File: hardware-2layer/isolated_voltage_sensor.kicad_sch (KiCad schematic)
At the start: 17 parts, among them U4 MCP41100, U5 LM358

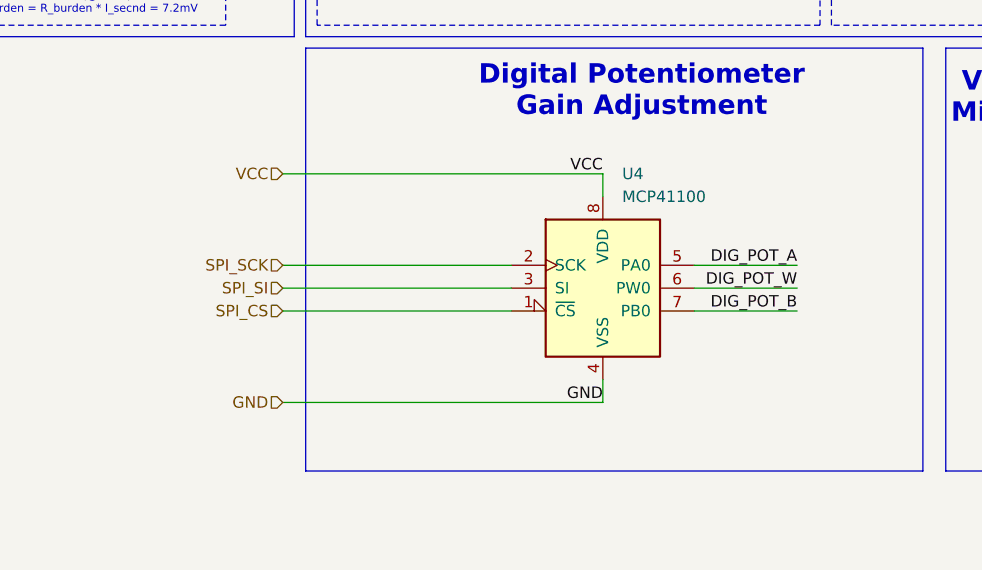
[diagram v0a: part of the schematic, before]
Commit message: updated board, last push before change to CRVR
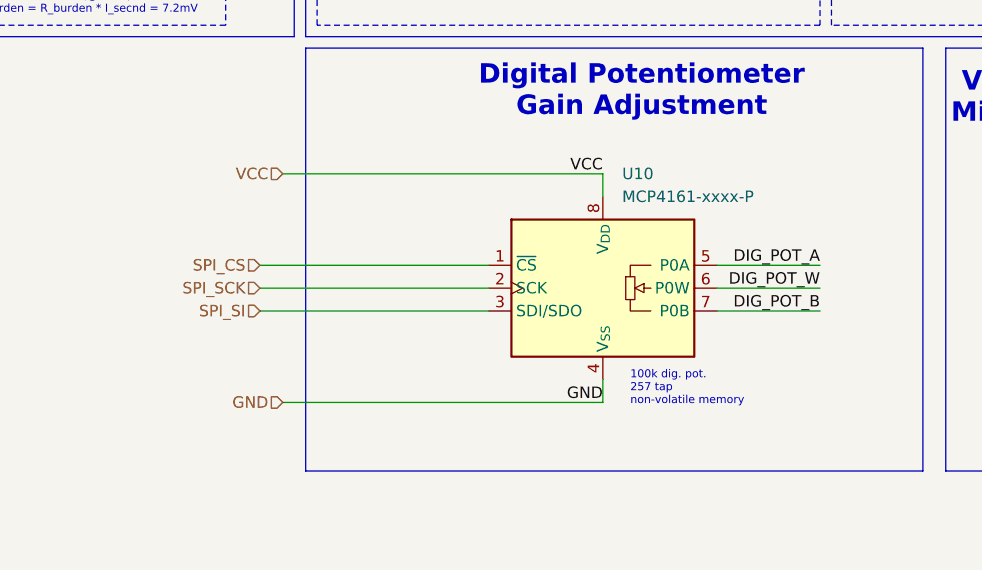
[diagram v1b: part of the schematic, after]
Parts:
- removed U4: MCP41100, symbol Potentiometer_Digital:MCP41100
- added U10: MCP4161-xxxx-P, Package_DIP:DIP-8_W7.62mm, symbol Potentiometer_Digital:MCP4161-xxxx-P
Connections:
- net DIG_POT_A: now also U10.5 (P0A)
- net DIG_POT_W: now also U10.6 (P0W)
- net GND: now also U10.4 (V_{SS}), U10.7 (P0B)
- net SPI_CS: now also U10.1 (~{CS})
- net SPI_SCK: now also U10.2 (SCK)
- net SPI_SI: now also U10.3 (SDI/SDO)
- net VCC: now also U10.8 (V_{DD})
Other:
- note added: "100k dig. pot. 257 tap non-volatile memory"
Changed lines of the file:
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@@
+		)
+	)
+	(text "100k dig. pot.\n257 tap\nnon-volatile memory"
+		(exclude_from_sim no)
+		(at 147.828 149.606 0)
+		(effects
+			(font
+				(size 0.889 0.889)
+				(thickness 0.0794)
+			)
+			(justify left)
 		)
 	)
@@
 	(wire
 		(pts
-			(xy 166.37 135.89) (xy 154.94 135.89)
+			(xy 168.91 135.89) (xy 157.48 135.89)
 		)
 		(stroke
@@
 	(wire
 		(pts
-			(xy 109.22 135.89) (xy 134.62 135.89)
+			(xy 106.68 138.43) (xy 132.08 138.43)
 		)
 		(stroke
@@
 	(wire
 		(pts
-			(xy 109.22 138.43) (xy 134.62 138.43)
+			(xy 106.68 140.97) (xy 132.08 140.97)
 		)
 		(stroke
@@
 	(wire
 		(pts
-			(xy 166.37 140.97) (xy 154.94 140.97)
+			(xy 168.91 140.97) (xy 157.48 140.97)
 		)
 		(stroke
@@
 	(wire
 		(pts
-			(xy 166.37 138.43) (xy 154.94 138.43)
-		)
-		(stroke
-			(width 0)
-			(type default)
-		)
-	)
-	(wire
-		(pts
-			(xy 109.22 140.97) (xy 134.62 140.97)
+			(xy 168.91 138.43) (xy 157.48 138.43)
+		)
+		(stroke
+			(width 0)
+			(type default)
+		)
+	)
+	(wire
+		(pts
+			(xy 106.68 135.89) (xy 132.08 135.89)
 		)
 		(stroke
@@
 	)
 	(label "DIG_POT_A"
-		(at 166.37 135.89 180)
+		(at 168.91 135.89 180)
 		(effects
 			(font
@@
 	)
 	(label "DIG_POT_W"
-		(at 166.37 138.43 180)
+		(at 168.91 138.43 180)
 		(effects
 			(font
@@
 	)
 	(label "DIG_POT_B"
-		(at 166.37 140.97 180)
+		(at 168.91 140.97 180)
 		(effects
 			(font
@@
 	(hierarchical_label "SPI_SI"
 		(shape input)
-		(at 109.22 138.43 180)
+		(at 106.68 140.97 180)
 		(effects
 			(font
@@
 	(hierarchical_label "SPI_SCK"
 		(shape input)
-		(at 109.22 135.89 180)
+		(at 106.68 138.43 180)
 		(effects
 			(font
@@
 	(hierarchical_label "SPI_CS"
 		(shape input)
-		(at 109.22 140.97 180)
+		(at 106.68 135.89 180)
 		(effects
 			(font
@@
 	)
 	(symbol
+		(lib_id "Potentiometer_Digital:MCP4161-xxxx-P")
+		(at 144.78 138.43 0)
+		(unit 1)
+		(exclude_from_sim no)
+		(in_bom yes)
+		(on_board yes)
+		(dnp no)
+		(fields_autoplaced yes)
+		(property "Reference" "U10"
+			(at 146.9233 125.73 0)
+			(effects
+				(font
+					(size 1.27 1.27)
+				)
+				(justify left)
+			)
+		)
+		(property "Value" "MCP4161-xxxx-P"
+			(at 146.9233 128.27 0)
+			(effects
+				(font
+					(size 1.27 1.27)
+				)
+				(justify left)
+			)
+		)
+		(property "Footprint" "Package_DIP:DIP-8_W7.62mm"
+			(at 144.78 158.75 0)
+			(effects
+				(font
+					(size 1.27 1.27)
+				)
+				(hide yes)
+			)
+		)
+		(property "Datasheet" "https://ww1.microchip.com/downloads/aemDocuments/documents/OTH/ProductDocuments/DataSheets/22059b.pdf"
+			(at 144.78 161.29 0)
+			(effects
+				(font
+					(size 1.27 1.27)
+				)
+				(hide yes)
+			)
+		)
+		(property "Description" "Single Digital Potentiometer, SPI interface, 257 taps, 5/10/50/100 kohm, non-volatile memory"
+			(at 144.78 163.83 0)
+			(effects
+				(font
+					(size 1.27 1.27)
+				)
+				(hide yes)
+			)
+		)
+		(pin "1"
+		)
+		(pin "2"
+		)
+		(pin "3"
+		)
+		(pin "6"
+		)
+		(pin "4"
+		)
+		(pin "7"
+		)
+		(pin "8"
+		)
+		(pin "5"
+		)
+		(instances
+			(project "BREAD_Slice"
+				(path "/66043bca-a260-4915-9fce-8a51d324c687/7d381b9c-9d38-42fd-86f2-ccc6e97560d8"
+					(reference "U11")
+					(unit 1)
+				)
+				(path "/66043bca-a260-4915-9fce-8a51d324c687/a1865804-4053-4b6c-b725-3b172b655c52"
+					(reference "U10")
+					(unit 1)
+				)
+			)
+		)
+	)
+	(symbol
 		(lib_id "Device:R")
 		(at 194.31 135.89 180)
@@
 					(unit 1)
 				)
-			)
-		)
-	)
-	(symbol
-		(lib_id "Potentiometer_Digital:MCP41100")
-		(at 144.78 138.43 0)
-		(unit 1)
-		(exclude_from_sim no)
-		(in_bom yes)
-		(on_board yes)
-		(dnp no)
-		(fields_autoplaced yes)
-		(property "Reference" "U4"
-			(at 146.9233 125.73 0)
-			(effects
-				(font
-					(size 1.27 1.27)
-				)
-				(justify left)
-			)
-		)
-		(property "Value" "MCP41100"
-			(at 146.9233 128.27 0)
-			(effects
-				(font
-					(size 1.27 1.27)
-				)
-				(justify left)
-			)
-		)
-		(property "Footprint" ""
-			(at 144.78 138.43 0)
-			(effects
-				(font
-					(size 1.27 1.27)
-				)
-				(hide yes)
-			)
-		)
-		(property "Datasheet" "http://ww1.microchip.com/downloads/en/DeviceDoc/11195c.pdf"
-			(at 144.78 138.43 0)
-			(effects
-				(font
-					(size 1.27 1.27)
-				)
-				(hide yes)
-			)
-		)
-		(property "Description" "Single Digital Potentiometer, SPI interface, 256 taps, 100 kohm"
-			(at 144.78 138.43 0)
-			(effects
-				(font
-					(size 1.27 1.27)
-				)
-				(hide yes)
-			)
-		)
-		(pin "2"
-		)
-		(pin "1"
-		)
-		(pin "8"
-		)
-		(pin "4"
-		)
-		(pin "5"
-		)
-		(pin "6"
-		)
-		(pin "3"
-		)
-		(pin "7"
-		)
-		(instances
-			(project "BREAD_Slice"
-				(path "/66043bca-a260-4915-9fce-8a51d324c687/7d381b9c-9d38-42fd-86f2-ccc6e97560d8"
-					(reference "U6")
-					(unit 1)
-				)
-				(path "/66043bca-a260-4915-9fce-8a51d324c687/a1865804-4053-4b6c-b725-3b172b655c52"
-					(reference "U4")
-					(unit 1)
-				)
